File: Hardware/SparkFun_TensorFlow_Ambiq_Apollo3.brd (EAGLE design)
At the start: 40 x 40 mm, 132 parts, among them J5 CORTEX_DEBUG_PTH, J6 CAMERA-OV7670, M1 MEMS_MIC, M2 MEMS_MIC, U1 AMBIQ-APOLLO3KBR, U2 LIS2DH12, U3 1.8V, U4 LMV358, Y1 32MHz, Y2 32.768kHz

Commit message: Updating components to SparkFun ibraries
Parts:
- C1, C11, C16, C18, C2, C28, C3, C5, C8: device ambiq:0402-TIGHT -> SparkFun-Capacitors:0402-TIGHT
- J6: device ambiq:FPC-24-AMPHENOL-SFV24R-1STE1HLF -> SparkFun-Connectors:FPC-24-AMPHENOL-SFV24R-1STE1HLF
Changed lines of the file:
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@@
 <attribute name="VALUE" x="25.1936" y="14.8102" size="0.6096" layer="27" font="vector" ratio="20" align="top-center"/>
 </element>
-<element name="C2" library="ambiq" package="0402-TIGHT" value="4.7uF" x="23.25" y="15.7" smashed="yes" rot="R270">
-<attribute name="DIGIKEY" value="1276-1056-1-ND" x="23.25" y="15.7" size="1.778" layer="27" font="vector" ratio="15" rot="R270" display="off"/>
+<element name="C2" library="SparkFun-Capacitors" package="0402-TIGHT" value="4.7uF" x="23.25" y="15.7" smashed="yes" rot="R270">
 <attribute name="NAME" x="23.812" y="15.7" size="0.6096" layer="25" font="vector" ratio="20" rot="R270" align="bottom-center"/>
+<attribute name="PROD_ID" value="CAP-14240" x="23.25" y="15.7" size="1.778" layer="27" rot="R270" display="off"/>
 <attribute name="VALUE" x="23.0066" y="13.7386" size="0.6096" layer="27" font="vector" ratio="20" rot="R90" align="top-center"/>
 </element>
@@
 <attribute name="VALUE" x="32.9162" y="33.016" size="0.6096" layer="27" font="vector" ratio="20" rot="R90" align="top-center"/>
 </element>
-<element name="C1" library="ambiq" package="0402-TIGHT" value="0.47uF" x="23.2746" y="20.5" smashed="yes" rot="MR180">
-<attribute name="DIGIKEY" value="1276-1479-2-ND" x="23.2746" y="20.5" size="1.778" layer="28" font="vector" ratio="15" rot="MR180" display="off"/>
+<element name="C1" library="SparkFun-Capacitors" package="0402-TIGHT" value="0.47uF" x="23.2746" y="20.5" smashed="yes" rot="MR180">
 <attribute name="NAME" x="23.2746" y="19.738" size="0.6096" layer="26" font="vector" ratio="20" rot="MR180" align="bottom-center"/>
+<attribute name="PROD_ID" value="CAP-14242" x="23.2746" y="20.5" size="1.778" layer="28" rot="MR180" display="off"/>
 <attribute name="VALUE" value="0.47uF" x="23.2746" y="21.262" size="0.6096" layer="28" font="vector" ratio="20" rot="MR180" align="top-center"/>
 </element>
-<element name="C3" library="ambiq" package="0402-TIGHT" value="2.2uF" x="23.273" y="19.35" smashed="yes" rot="MR0">
-<attribute name="DIGIKEY" value="1276-1462-2-ND" x="23.273" y="19.35" size="1.778" layer="28" rot="MR0" display="off"/>
+<element name="C3" library="SparkFun-Capacitors" package="0402-TIGHT" value="2.2uF" x="23.273" y="19.35" smashed="yes" rot="MR0">
 <attribute name="NAME" x="23.273" y="20.112" size="0.6096" layer="26" font="vector" ratio="20" rot="MR0" align="bottom-center"/>
+<attribute name="PROD_ID" value="CAP-14232" x="23.273" y="19.35" size="1.778" layer="28" rot="MR0" display="off"/>
+<attribute name="VALUE" x="23.273" y="18.788" size="0.6096" layer="28" font="vector" ratio="20" rot="MR0" align="top-center"/>
 <attribute name="VALUE" value="2.2uF" x="23.273" y="19.35" size="1.778" layer="28" rot="MR0" display="off"/>
-<attribute name="VALUE" x="23.273" y="18.788" size="0.6096" layer="28" font="vector" ratio="20" rot="MR0" align="top-center"/>
-</element>
-<element name="C5" library="ambiq" package="0402-TIGHT" value="2.2uF" x="25.25" y="17.7746" smashed="yes" rot="MR270">
-<attribute name="DIGIKEY" value="1276-1462-2-ND" x="25.25" y="17.7746" size="1.778" layer="28" rot="MR270" display="off"/>
+</element>
+<element name="C5" library="SparkFun-Capacitors" package="0402-TIGHT" value="2.2uF" x="25.25" y="17.7746" smashed="yes" rot="MR270">
 <attribute name="NAME" x="24.488" y="17.7746" size="0.6096" layer="26" font="vector" ratio="20" rot="MR270" align="bottom-center"/>
+<attribute name="PROD_ID" value="CAP-14232" x="25.25" y="17.7746" size="1.778" layer="28" rot="MR270" display="off"/>
+<attribute name="VALUE" x="25.812" y="17.7746" size="0.6096" layer="28" font="vector" ratio="20" rot="MR270" align="top-center"/>
 <attribute name="VALUE" value="2.2uF" x="25.25" y="17.7746" size="1.778" layer="28" rot="MR270" display="off"/>
-<attribute name="VALUE" x="25.812" y="17.7746" size="0.6096" layer="28" font="vector" ratio="20" rot="MR270" align="top-center"/>
-</element>
-<element name="C8" library="ambiq" package="0402-TIGHT" value="2.2uF" x="26.3" y="17.5" smashed="yes" rot="MR270">
-<attribute name="DIGIKEY" value="1276-1462-2-ND" x="26.3" y="17.5" size="1.778" layer="28" rot="MR270" display="off"/>
+</element>
+<element name="C8" library="SparkFun-Capacitors" package="0402-TIGHT" value="2.2uF" x="26.3" y="17.5" smashed="yes" rot="MR270">
 <attribute name="NAME" x="25.538" y="17.5" size="0.6096" layer="26" font="vector" ratio="20" rot="MR270" align="bottom-center"/>
+<attribute name="PROD_ID" value="CAP-14232" x="26.3" y="17.5" size="1.778" layer="28" rot="MR270" display="off"/>
+<attribute name="VALUE" x="26.862" y="17.5" size="0.6096" layer="28" font="vector" ratio="20" rot="MR270" align="top-center"/>
 <attribute name="VALUE" value="2.2uF" x="26.3" y="17.5" size="1.778" layer="28" rot="MR270" display="off"/>
-<attribute name="VALUE" x="26.862" y="17.5" size="0.6096" layer="28" font="vector" ratio="20" rot="MR270" align="top-center"/>
 </element>
 <element name="C12" library="ambiq" package="0402-TIGHT" value="1.0uF" x="23.7" y="18.25" smashed="yes" rot="MR0">
@@
 <attribute name="VALUE" x="27.5734" y="20.1" size="0.6096" layer="28" font="vector" ratio="20" rot="MR90" align="top-center"/>
 </element>
-<element name="C11" library="ambiq" package="0402-TIGHT" value="47nF" x="28.9" y="18.6" smashed="yes" rot="MR180">
-<attribute name="DIGIKEY" value="311-1717-2-ND" x="28.9" y="18.6" size="1.778" layer="28" font="vector" ratio="15" rot="MR180" display="off"/>
+<element name="C11" library="SparkFun-Capacitors" package="0402-TIGHT" value="47nF" x="28.9" y="18.6" smashed="yes" rot="MR180">
 <attribute name="NAME" x="28.9" y="17.838" size="0.6096" layer="26" font="vector" ratio="20" rot="MR180" align="bottom-center"/>
+<attribute name="PROD_ID" value="CAP-14243" x="28.9" y="18.6" size="1.778" layer="28" rot="MR180" display="off"/>
 <attribute name="VALUE" x="28.9" y="19.362" size="0.6096" layer="28" font="vector" ratio="20" rot="MR180" align="top-center"/>
 </element>
-<element name="C16" library="ambiq" package="0402-TIGHT" value="2.2uF" x="23.7" y="17.2" smashed="yes" rot="MR0">
-<attribute name="DIGIKEY" value="1276-1462-2-ND" x="23.7" y="17.2" size="1.778" layer="28" rot="MR0" display="off"/>
+<element name="C16" library="SparkFun-Capacitors" package="0402-TIGHT" value="2.2uF" x="23.7" y="17.2" smashed="yes" rot="MR0">
 <attribute name="NAME" x="23.7" y="17.962" size="0.6096" layer="26" font="vector" ratio="20" rot="MR0" align="bottom-center"/>
+<attribute name="PROD_ID" value="CAP-14232" x="23.7" y="17.2" size="1.778" layer="28" rot="MR0" display="off"/>
+<attribute name="VALUE" x="23.7" y="16.638" size="0.6096" layer="28" font="vector" ratio="20" rot="MR0" align="top-center"/>
 <attribute name="VALUE" value="2.2uF" x="23.7" y="17.2" size="1.778" layer="28" rot="MR0" display="off"/>
-<attribute name="VALUE" x="23.7" y="16.638" size="0.6096" layer="28" font="vector" ratio="20" rot="MR0" align="top-center"/>
 </element>
 <element name="C17" library="ambiq" package="0402-TIGHT" value="DNP" x="30.1" y="17.5" smashed="yes" rot="R270">
@@
 <attribute name="VALUE" x="31.3512" y="18.4014" size="0.6096" layer="27" font="vector" ratio="20" rot="R180" align="top-center"/>
 </element>
-<element name="C18" library="ambiq" package="0402-TIGHT" value="0.5pF" x="32.6314" y="17.5" smashed="yes" rot="R270">
-<attribute name="DIGIKEY" value="399-16299-1-ND" x="32.6314" y="17.5" size="1.778" layer="27" font="vector" ratio="15" rot="R270" display="off"/>
+<element name="C18" library="SparkFun-Capacitors" package="0402-TIGHT" value="0.5pF" x="32.6314" y="17.5" smashed="yes" rot="R270">
 <attribute name="NAME" x="33.1934" y="17.5" size="0.6096" layer="25" font="vector" ratio="20" rot="R270" align="bottom-center"/>
+<attribute name="PROD_ID" value="CAP-14240" x="32.6314" y="17.5" size="1.778" layer="27" rot="R270" display="off"/>
 <attribute name="VALUE" x="32.6396" y="16.6008" size="0.6096" layer="27" font="vector" ratio="20" align="top-center"/>
 </element>
@@
 <attribute name="VALUE" x="8.001" y="1.0922" size="0.6096" layer="27" font="vector" ratio="20" rot="R180" align="bottom-center"/>
 </element>
-<element name="J6" library="ambiq" package="FPC-24-AMPHENOL-SFV24R-1STE1HLF" value="CAMERA-OV7670" x="20" y="37" smashed="yes" rot="R180">
+<element name="J6" library="SparkFun-Connectors" package="FPC-24-AMPHENOL-SFV24R-1STE1HLF" value="CAMERA-OV7670" x="20" y="37" smashed="yes" rot="R180">
 <attribute name="DIGIKEY" value="609-4320-2-ND" x="20" y="37" size="1.778" layer="27" rot="R180" display="off"/>
 <attribute name="NAME" x="20" y="39.3368" size="0.6096" layer="25" font="vector" ratio="20" rot="R180" align="top-center"/>
+<attribute name="PROD_ID" value="CONN-14233" x="20" y="37" size="1.778" layer="27" rot="R180" display="off"/>
 <attribute name="VALUE" x="20" y="37" size="0.6096" layer="27" font="vector" ratio="20" rot="R180" align="center"/>
 </element>
@@
 <element name="TP1" library="SparkFun-Connectors" package="PAD.03X.05" value="TEST-POINT3X5" x="31.75" y="35.56" smashed="yes" rot="MR0"/>
 <element name="TP2" library="SparkFun-Connectors" package="PAD.03X.05" value="TEST-POINT3X5" x="34.29" y="35.56" smashed="yes" rot="MR0"/>
-<element name="C28" library="ambiq" package="0402-TIGHT" value="1.0nF" x="1.8" y="31" smashed="yes" rot="R90">
-<attribute name="DIGIKEY" value="311-1036-2-ND" x="1.8" y="31" size="1.778" layer="27" rot="R90" display="off"/>
+<element name="C28" library="SparkFun-Capacitors" package="0402-TIGHT" value="1.0nF" x="1.8" y="31" smashed="yes" rot="R90">
 <attribute name="NAME" x="1.238" y="31" size="0.6096" layer="25" font="vector" ratio="20" rot="R90" align="bottom-center"/>
+<attribute name="PROD_ID" value="CAP-14280" x="1.8" y="31" size="1.778" layer="27" rot="R90" display="off"/>
 <attribute name="VALUE" value="1.0nF" x="2.362" y="31" size="0.6096" layer="27" font="vector" ratio="20" rot="R90" align="top-center"/>
 </element>

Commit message: Continue adding parts from SparkFun library
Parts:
- L1: value 2.2uH -> 2.2μH; device ambiq:0805-WIDE -> SparkFun-Coils:0805-WIDE
- L2: value 1.0uH -> 1.0μH; device ambiq:0805-WIDE -> SparkFun-Coils:0805-WIDE
- L3: value 2.7nH -> 2.7nH/?%/900mA/70mOhm; device ambiq:0402-TIGHT -> SparkFun-Coils:0402-TIGHT
- L4: value 2.0nH -> 2nH/?%/200mA/300mOhm; device ambiq:0402-TIGHT -> SparkFun-Coils:0402-TIGHT
- M1, M2: device ambiq:SPW2430HR5H-B -> SparkFun-Sensors:SPW2430HR5H-B
- R18: device ambiq:0402-TIGHT -> SparkFun-Resistors:0402-TIGHT
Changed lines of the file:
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@@
 <attribute name="VALUE" x="1.2096" y="31" size="0.6096" layer="27" font="vector" ratio="20" rot="R90" align="top-center"/>
 </element>
-<element name="L1" library="ambiq" package="0805-WIDE" value="2.2uH" x="21.7" y="18" smashed="yes" rot="R90">
-<attribute name="DIGIKEY" value="490-17728-2-ND" x="21.7" y="18" size="1.778" layer="27" rot="R90" display="off"/>
+<element name="L1" library="SparkFun-Coils" package="0805-WIDE" value="2.2μH" x="21.7" y="18" smashed="yes" rot="R90">
 <attribute name="NAME" x="20.611" y="18" size="0.6096" layer="25" font="vector" ratio="20" rot="R90" align="bottom-center"/>
-<attribute name="VALUE" x="20.6704" y="17.9918" size="0.6096" layer="27" font="vector" ratio="20" rot="R270" align="top-center"/>
-</element>
-<element name="L2" library="ambiq" package="0805-WIDE" value="1.0uH" x="25.2" y="15.8" smashed="yes" rot="R180">
-<attribute name="DIGIKEY" value="587-2903-2-ND" x="25.2" y="15.8" size="1.778" layer="27" font="vector" ratio="15" rot="R180" display="off"/>
+<attribute name="PROD_ID" value="NDUC-14234" x="21.7" y="18" size="1.778" layer="27" rot="R90" display="off"/>
+<attribute name="VALUE" value="2.2μH" x="20.6704" y="17.9918" size="0.6096" layer="27" font="vector" ratio="20" rot="R270" align="top-center"/>
+</element>
+<element name="L2" library="SparkFun-Coils" package="0805-WIDE" value="1.0μH" x="25.2" y="15.8" smashed="yes" rot="R180">
 <attribute name="NAME" x="25.2" y="14.711" size="0.6096" layer="25" font="vector" ratio="20" rot="R180" align="bottom-center"/>
-<attribute name="VALUE" x="25.1936" y="14.8102" size="0.6096" layer="27" font="vector" ratio="20" align="top-center"/>
+<attribute name="PROD_ID" value="NDUC-14237" x="25.2" y="15.8" size="1.778" layer="27" rot="R180" display="off"/>
+<attribute name="VALUE" value="1.0μH" x="25.1936" y="14.8102" size="0.6096" layer="27" font="vector" ratio="20" align="top-center"/>
 </element>
 <element name="C2" library="SparkFun-Capacitors" package="0402-TIGHT" value="4.7uF" x="23.25" y="15.7" smashed="yes" rot="R270">
@@
 <attribute name="VALUE" x="29.665" y="17.7286" size="0.6096" layer="27" font="vector" ratio="20" rot="R270" align="top-center"/>
 </element>
-<element name="L3" library="ambiq" package="0402-TIGHT" value="2.7nH" x="31.3614" y="18" smashed="yes">
-<attribute name="DIGIKEY" value="445-172420-1-ND" x="31.3614" y="18" size="1.778" layer="27" font="vector" ratio="15" display="off"/>
+<element name="L3" library="SparkFun-Coils" package="0402-TIGHT" value="2.7nH/?%/900mA/70mOhm" x="31.3614" y="18" smashed="yes">
 <attribute name="NAME" x="31.3614" y="18.562" size="0.6096" layer="25" font="vector" ratio="20" align="bottom-center"/>
-<attribute name="VALUE" x="31.3512" y="18.4014" size="0.6096" layer="27" font="vector" ratio="20" rot="R180" align="top-center"/>
+<attribute name="PROD_ID" value="NDUC-14236" x="31.3614" y="18" size="1.778" layer="27" display="off"/>
+<attribute name="VALUE" value="2.7nH/?%/900mA/70mOhm" x="31.3512" y="18.4014" size="0.6096" layer="27" font="vector" ratio="20" rot="R180" align="top-center"/>
 </element>
 <element name="C18" library="SparkFun-Capacitors" package="0402-TIGHT" value="0.5pF" x="32.6314" y="17.5" smashed="yes" rot="R270">
@@
 <attribute name="VALUE" x="32.6396" y="16.6008" size="0.6096" layer="27" font="vector" ratio="20" align="top-center"/>
 </element>
-<element name="L4" library="ambiq" package="0402-TIGHT" value="2.0nH" x="33.9014" y="18" smashed="yes">
-<attribute name="DIGIKEY" value="490-6752-1-ND" x="33.9014" y="18" size="1.778" layer="27" font="vector" ratio="15" display="off"/>
+<element name="L4" library="SparkFun-Coils" package="0402-TIGHT" value="2nH/?%/200mA/300mOhm" x="33.9014" y="18" smashed="yes">
 <attribute name="NAME" x="33.9014" y="18.562" size="0.6096" layer="25" font="vector" ratio="20" align="bottom-center"/>
-<attribute name="VALUE" x="34.3738" y="18.4014" size="0.6096" layer="27" font="vector" ratio="20" rot="R180" align="top-center"/>
+<attribute name="PROD_ID" value="NDUC-14238" x="33.9014" y="18" size="1.778" layer="27" display="off"/>
+<attribute name="VALUE" value="2nH/?%/200mA/300mOhm" x="34.3738" y="18.4014" size="0.6096" layer="27" font="vector" ratio="20" rot="R180" align="top-center"/>
 </element>
 <element name="A1" library="ambiq" package="ANT-2.4GHZ-3.2X1.6X1.2MM" value="2.4GHZ-3.2X1.6MM" x="38.128" y="16.3" smashed="yes" rot="R270">
@@
 <attribute name="VALUE" x="22.5762" y="14.5316" size="0.6096" layer="27" font="vector" ratio="20" rot="R270" align="top-center"/>
 </element>
-<element name="M1" library="ambiq" package="SPW2430HR5H-B" value="MEMS_MIC" x="8" y="37" smashed="yes" rot="R180">
+<element name="M1" library="SparkFun-Sensors" package="SPW2430HR5H-B" value="MEMS_MIC" x="8" y="37" smashed="yes" rot="R180">
 <attribute name="DIGIKEY" value="423-1394-2-ND" x="8" y="37" size="1.778" layer="27" rot="R180" display="off"/>
 <attribute name="NAME" x="9.524" y="37" size="0.6096" layer="25" font="vector" ratio="20" rot="R270" align="bottom-center"/>
+<attribute name="PROD_ID" value="COMP-14230" x="8" y="37" size="1.778" layer="27" rot="R180" display="off"/>
 <attribute name="VALUE" x="7.9932" y="38.863" size="0.6096" layer="27" font="vector" ratio="20" align="bottom-center"/>
 </element>
-<element name="M2" library="ambiq" package="SPW2430HR5H-B" value="MEMS_MIC" x="8" y="3" smashed="yes">
+<element name="M2" library="SparkFun-Sensors" package="SPW2430HR5H-B" value="MEMS_MIC" x="8" y="3" smashed="yes">
 <attribute name="DIGIKEY" value="423-1394-2-ND" x="8" y="3" size="1.778" layer="27" display="off"/>
 <attribute name="NAME" x="6.476" y="3" size="0.6096" layer="25" font="vector" ratio="20" rot="R90" align="bottom-center"/>
+<attribute name="PROD_ID" value="COMP-14230" x="8" y="3" size="1.778" layer="27" display="off"/>
 <attribute name="VALUE" x="8.001" y="1.0922" size="0.6096" layer="27" font="vector" ratio="20" rot="R180" align="bottom-center"/>
 </element>
@@
 <attribute name="VALUE" x="16.004" y="18.1236" size="0.6096" layer="27" font="vector" ratio="20" align="top-center"/>
 </element>
-<element name="R18" library="ambiq" package="0402-TIGHT" value="22k" x="16" y="19.5" smashed="yes">
-<attribute name="DIGIKEY" value="311-22.0KLRTR-ND" x="16" y="19.5" size="1.778" layer="27" display="off"/>
+<element name="R18" library="SparkFun-Resistors" package="0402-TIGHT" value="22k" x="16" y="19.5" smashed="yes">
 <attribute name="NAME" x="16" y="20.062" size="0.6096" layer="25" font="vector" ratio="20" align="bottom-center"/>
+<attribute name="PROD_ID" value="RES-14281" x="16" y="19.5" size="1.778" layer="27" display="off"/>
 <attribute name="VALUE" value="22k" x="16.9014" y="19.5052" size="0.6096" layer="27" font="vector" ratio="20" rot="R90" align="top-center"/>
 </element>

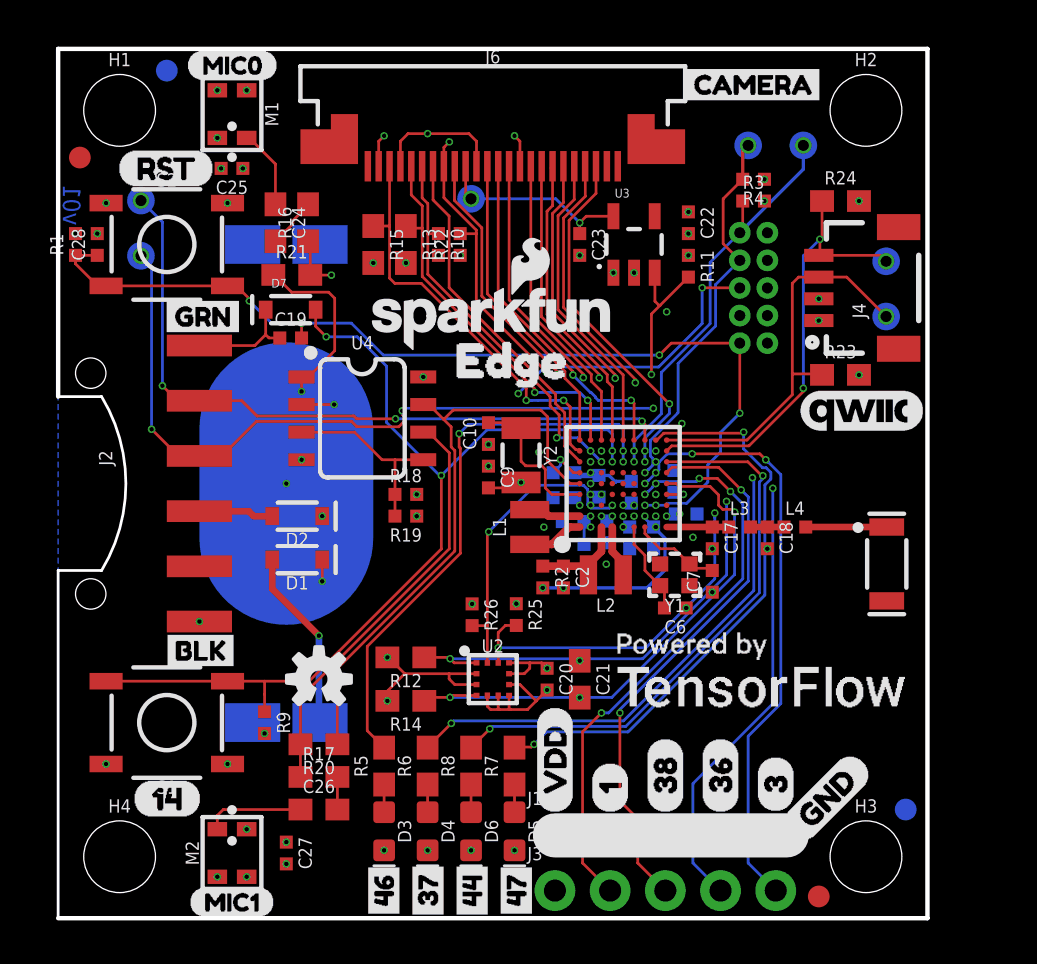
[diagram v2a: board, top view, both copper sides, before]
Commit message: Finish converting parts to SparkFun library
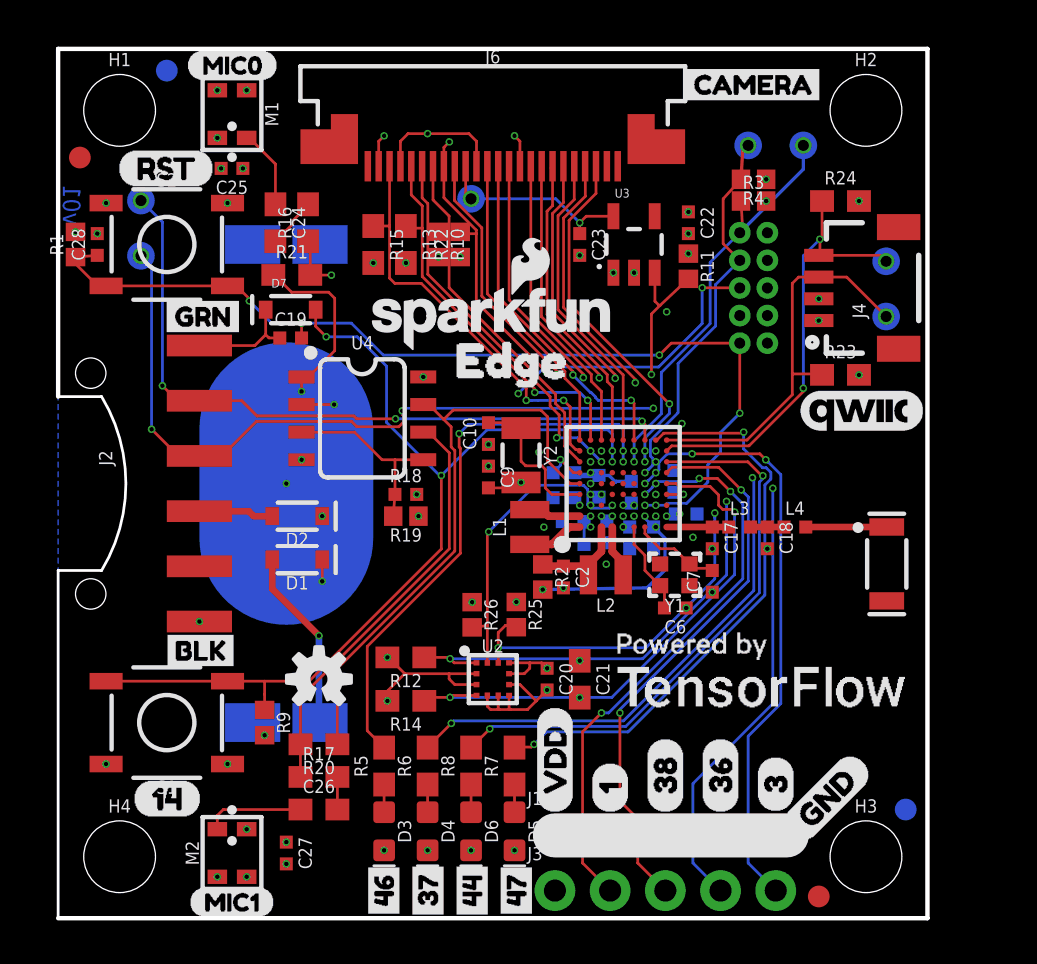
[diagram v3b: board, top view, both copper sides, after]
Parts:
- R1, R10, R11, R19, R2, R22, R25, R26, R3, R4, R9: device ambiq:0402-TIGHT -> SparkFun-Resistors:0402
- U1: device ambiq:BGA-81-5X5MM -> SparkFun-IC-Microcontroller:BGA-81-5X5MM
- U2: device ambiq:LGA-12-LISDH12 -> SparkFun-Sensors:LGA-12-LISDH12
- U3: device ambiq:SOT23-5 -> SparkFun-IC-Power:SOT23-5

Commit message: Moving designators for asm sheet
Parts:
- D7: value 250mA/100V -> DNP
- R9: value 10k -> 100k
